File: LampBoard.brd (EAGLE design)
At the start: 100 x 39.4 mm, 25 parts, among them IC1 MEGA8-AI, J1 70543-04, J2 70543-05, T1 BTA25

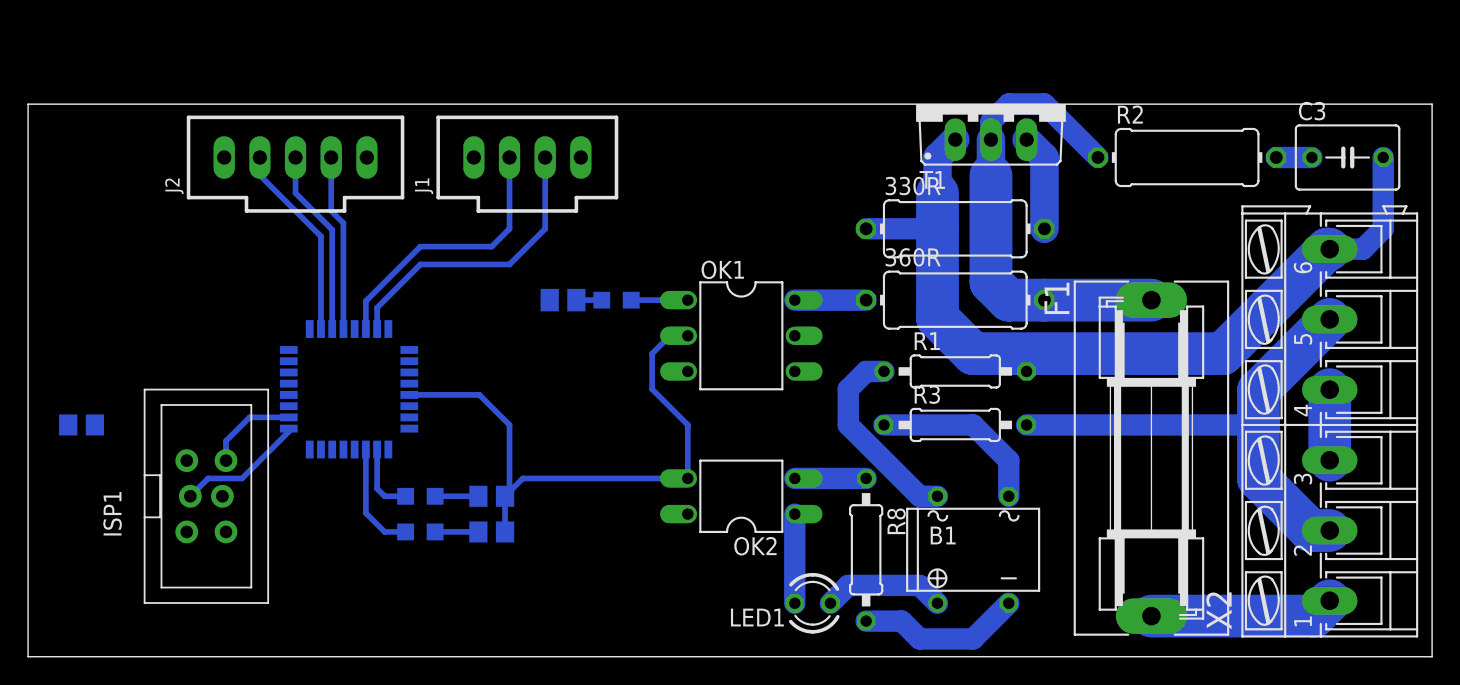
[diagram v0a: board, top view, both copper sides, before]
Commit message: AC section routed
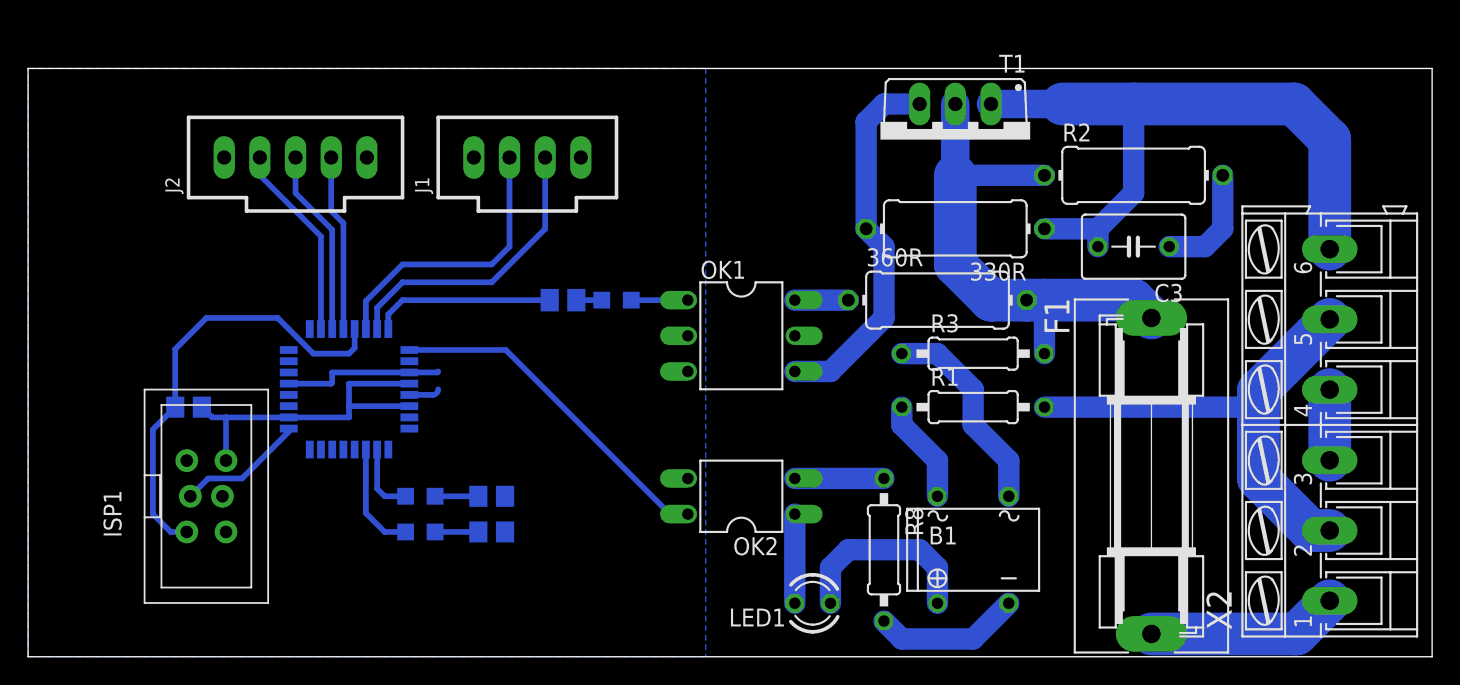
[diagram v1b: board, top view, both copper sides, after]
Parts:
- moved C3 16.5 mm to (78.7, 29.2), turned to 180 degrees
- moved R4 7.73 mm to (11.4, 17.8), turned to 180 degrees
- moved R3 5.24 mm to (67.3, 21.6)
- moved R2 4.02 mm to (78.7, 34.3)
- moved T1 3.59 mm to (66.0, 36.8), turned to 180 degrees
- moved R1 2.84 mm to (67.3, 17.8)
- moved 360R 1.27 mm to (64.8, 25.4)
- moved R8 1.27 mm to (61.0, 7.62)
- moved F1 1.27 mm to (80.0, 12.9)
- turned 330R to 180 degrees
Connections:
- net L_FUSED: now also R3.2; no longer R1.2
- net N: now also R1.2; no longer R3.2
- net SWITCH: now also IC1.32; no longer IC1.13
- net ZERO: now also IC1.1; no longer IC1.32
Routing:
- net RESET: track 0.00 -> 31.6 mm
- net GND: track 42.3 -> 14.9 mm
- net ZERO: track 0.00 -> 24.7 mm
- net N$3: track 6.88 -> 26.8 mm
- net +5V: track 6.56 -> 24.8 mm
- net SWITCH: track 0.00 -> 13.0 mm
- net LAMP: track 59.9 -> 48.0 mm
- net 22K: track 14.1 -> 7.40 mm
- net N$1: track 2.54 -> 8.15 mm
- net N$8: track 8.67 -> 13.8 mm
- net L_FUSED: track 33.1 -> 37.1 mm
- net N$5: track 12.5 -> 14.8 mm
- net N$7: track 5.08 -> 6.35 mm
- net N$11: track 11.7 -> 10.5 mm
- net N$2: track 5.08 -> 3.81 mm
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- added copper zone on layer 16, net GND
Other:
- board size 100 x 39.4 mm -> 100 x 41.9 mm

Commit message: Routing, refacotring
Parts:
- added H1: MOUNT-PAD-ROUND4.5, holes:4,5-PAD
- added H2, H3: MOUNT-HOLE4.5, holes:4,5
- LED2, LED3, LED4: device led:CHIPLED_0805 -> led:LED3MM
- moved R7 9.67 mm to (24.1, 5.08), turned to 90 degrees
- moved R6 7.41 mm to (29.2, 5.08), turned to 90 degrees
- moved LED3 3.81 mm to (24.1, 8.89), turned to 270 degrees
- moved LED4 2.84 mm to (29.2, 8.89), turned to 270 degrees
- moved R2 2.84 mm to (76.2, 35.6)
- moved 330R 1.80 mm to (64.8, 31.8)
- moved R5 1.80 mm to (36.8, 26.7)
- moved 360R 1.27 mm to (64.8, 26.7)
- moved LED2 1.27 mm to (41.9, 26.7), turned to 180 degrees
- moved T1 1.27 mm to (66.0, 38.1)
- moved B1 1.27 mm to (67.3, 8.89)
- moved R8 1.27 mm to (61.0, 8.89)
- moved LED1 1.27 mm to (55.9, 5.08)
- moved C3 1.27 mm to (78.7, 30.5)
- moved F1 1.27 mm to (80.0, 14.1)
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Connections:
- net N$14: now also LED4.K; no longer LED4.C
- net N$15: now also LED3.K; no longer LED3.C
- net N$6: now also LED2.K; no longer LED2.C
- net PE: now also H1.B4,5
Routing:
- net PE: track 5.03 -> 45.5 mm
- net +5V: track 24.8 -> 46.2 mm
- net N$13: track 5.04 -> 9.16 mm
- net N$3: track 26.8 -> 29.6 mm
- net L_FUSED: track 37.1 -> 34.4 mm
- net N$1: track 8.15 -> 5.61 mm
- net N$10: track 7.91 -> 5.90 mm
- net N$15: track 3.08 -> 1.59 mm
- net N$14: track 3.08 -> 1.59 mm
- net LAMP: track 48.0 -> 46.6 mm
- net N$5: track 14.8 -> 13.5 mm
- net 22K: track 7.40 -> 6.13 mm
- net SWITCH: track 13.0 -> 11.7 mm
- net N$9: track 1.81 -> 2.86 mm
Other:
- board size 100 x 41.9 mm -> 100 x 44.4 mm

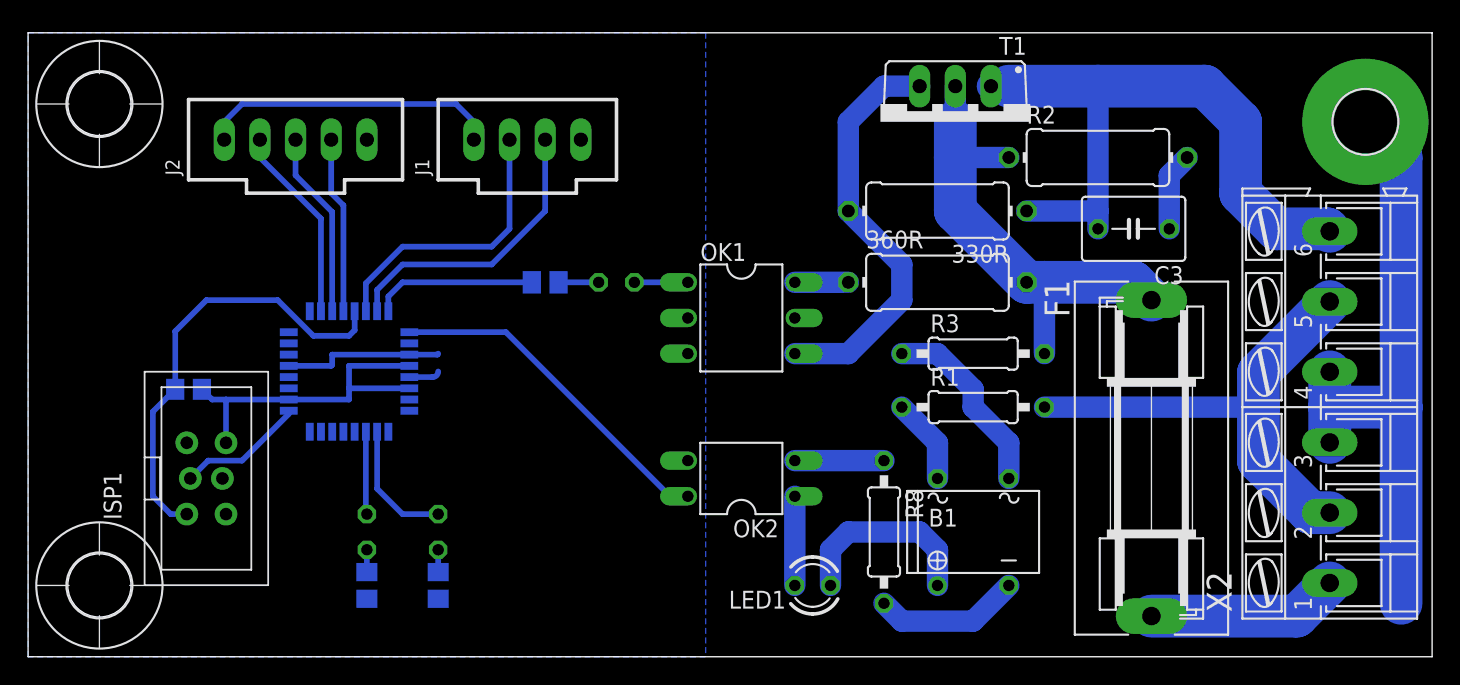
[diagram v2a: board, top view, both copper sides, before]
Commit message: Procesor moved away from Power board
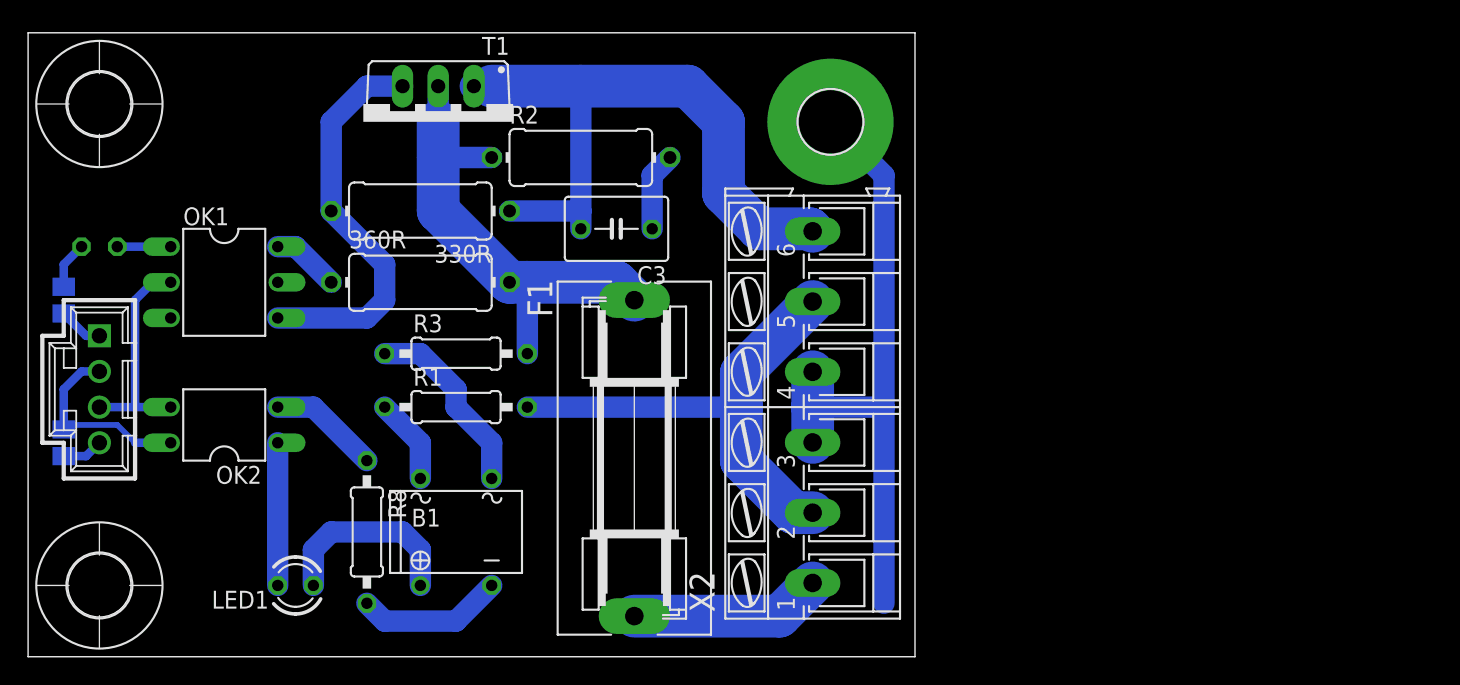
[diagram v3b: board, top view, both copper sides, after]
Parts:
- removed IC1: MEGA8-AI, atmel:TQFP32-08
- removed ISP1: AVRISP-BOX, adafruit:AVRISP-BOX
- removed J1: 70543-04, con-molex-c-grid:70543-04
- removed J2: 70543-05, con-molex-c-grid:70543-05
- removed LED3, LED4: (no value), led:LED3MM
- removed R6, R7: (no value), rcl:R0805
- added X1: HEADER_POS4_70543, con-molex-c-grid-sl:70543-POS4
- R1, R8: value 1M -> 22k
- R3: value 100R -> 22k
- R4: value (none) -> 1k; device rcl:R0805 -> rcl:M0805
- moved H1 38.1 mm to (57.1, 38.1)
- moved OK2 37.0 mm to (14.0, 16.5)
- moved LED2 36.9 mm to (5.08, 29.2)
- moved OK1 36.9 mm to (14.0, 26.7)
- moved F1 36.8 mm to (43.2, 14.1)
- moved R2 36.8 mm to (39.4, 35.6)
- moved T1 36.8 mm to (29.2, 38.1)
- moved 330R 36.8 mm to (27.9, 31.8)
- moved 360R 36.8 mm to (27.9, 26.7)
- moved B1 36.8 mm to (30.5, 8.89)
- moved C3 36.8 mm to (41.9, 30.5)
- moved LED1 36.8 mm to (19.1, 5.08)
- moved R1 36.8 mm to (30.5, 17.8)
- moved R3 36.8 mm to (30.5, 21.6)
- moved R8 36.8 mm to (24.1, 8.89)
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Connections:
- removed net IRQ: IC1.26, J2.2
- removed net MISO: IC1.16, ISP1.1
- removed net MOSI: IC1.15, ISP1.4
- removed net N$10: IC1.11, LED3.A
- removed net N$13: IC1.10, LED4.A
- removed net N$14: LED4.K, R6.2
- removed net N$15: LED3.K, R7.2
- removed net RESET: IC1.29, ISP1.5, R4.1
- removed net RXD: IC1.30, J1.2
- removed net SCK: IC1.17, ISP1.3
- removed net SCL: IC1.28, J2.4
- removed net SDA: IC1.27, J2.3
- removed net TXD: IC1.31, J1.3
- net +5V: now also X1.P$4; no longer IC1.18, IC1.4, IC1.6, ISP1.2, J1.1, J2.1
- net GND: now also X1.P$3; no longer IC1.21, IC1.3, IC1.5, ISP1.6, J1.4, J2.5, R6.1, R7.1
- net SWITCH: now also X1.P$1; no longer IC1.32
- net ZERO: now also R4.1, X1.P$2; no longer IC1.1
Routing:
- net +5V: track 46.2 -> 2.93 mm
- net RESET: track 31.6 -> 0.00 mm
- net TXD: track 20.9 -> 0.00 mm
- net RXD: track 20.2 -> 0.00 mm
- net IRQ: track 14.0 -> 0.00 mm
- net SDA: track 13.3 -> 0.00 mm
- net SCL: track 12.6 -> 0.00 mm
- net ZERO: track 24.7 -> 14.2 mm
- net N$13: track 9.16 -> 0.00 mm
- net SCK: track 9.14 -> 0.00 mm
- net SWITCH: track 11.7 -> 3.20 mm
- net N$10: track 5.90 -> 0.00 mm
- net N$4: track 6.35 -> 10.2 mm
- net N$15: track 1.59 -> 0.00 mm
- net N$14: track 1.59 -> 0.00 mm
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- removed copper zone on layer 16, net GND
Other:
- board size 100 x 44.4 mm -> 63.2 x 44.4 mm
